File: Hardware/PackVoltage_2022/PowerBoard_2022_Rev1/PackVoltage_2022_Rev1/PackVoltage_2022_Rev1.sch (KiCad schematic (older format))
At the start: 20 parts

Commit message: added andersons
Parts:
- added Conn? (x2): M1, symbol MRDT_Connectors:AndersonPP
- added Conn? (x2): M2, symbol MRDT_Connectors:AndersonPP
- added Conn? (x2): M3, symbol MRDT_Connectors:AndersonPP
- added Conn? (x2): M4, symbol MRDT_Connectors:AndersonPP
- added Conn? (x2): M5, symbol MRDT_Connectors:AndersonPP
- added Conn? (x2): M6, symbol MRDT_Connectors:AndersonPP
- added Conn? (x2): Spare, symbol MRDT_Connectors:AndersonPP
- C? (x4): value CP1 -> 470uF
- D? (x2): value D -> 1.5KE36A+
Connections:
- net GND: now also Conn?.1 (GND), Conn?.1 (GND), Conn?.1 (GND), Conn?.1 (GND), Conn?.1 (GND), Conn?.1 (GND), Conn?.1 (GND)
- new net Anderson_M1: Conn?.4 (PV+)
- new net Anderson_M2: Conn?.4 (PV+)
- new net Anderson_M3: Conn?.4 (PV+)
- new net Anderson_M4: Conn?.4 (PV+)
- new net Anderson_M5: Conn?.4 (PV+)
- new net Anderson_M6: Conn?.4 (PV+)
- new net Anderson_Spare: Conn?.4 (PV+)
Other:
- moved on the sheet: C?, D?, R?

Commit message: fixed anderson tags
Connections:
- net Anderson_M1 renamed MOTORS/Anderson_M1
- net Anderson_M2 renamed MOTORS/Anderson_M2
- net Anderson_M3 renamed MOTORS/Anderson_M3
- net Anderson_M4 renamed MOTORS/Anderson_M4
- net Anderson_M5 renamed MOTORS/Anderson_M5
- net Anderson_M6 renamed MOTORS/Anderson_M6
- net Anderson_Spare renamed MOTORS/Anderson_Spare
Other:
- moved on the sheet: Conn?A, Conn?D

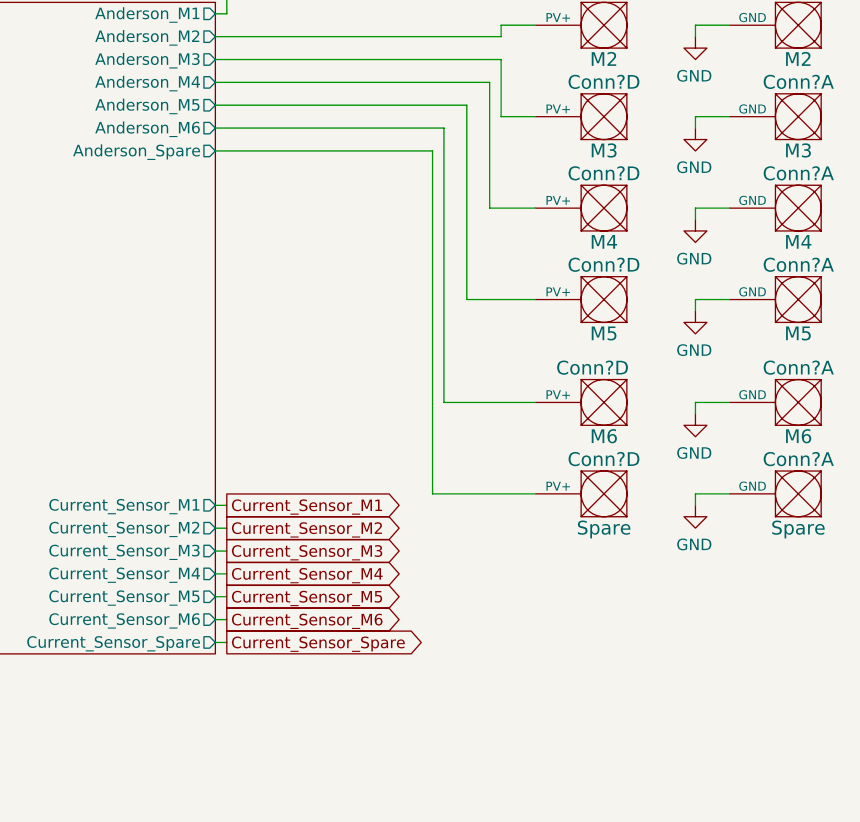
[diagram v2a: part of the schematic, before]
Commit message: added 12V anderson
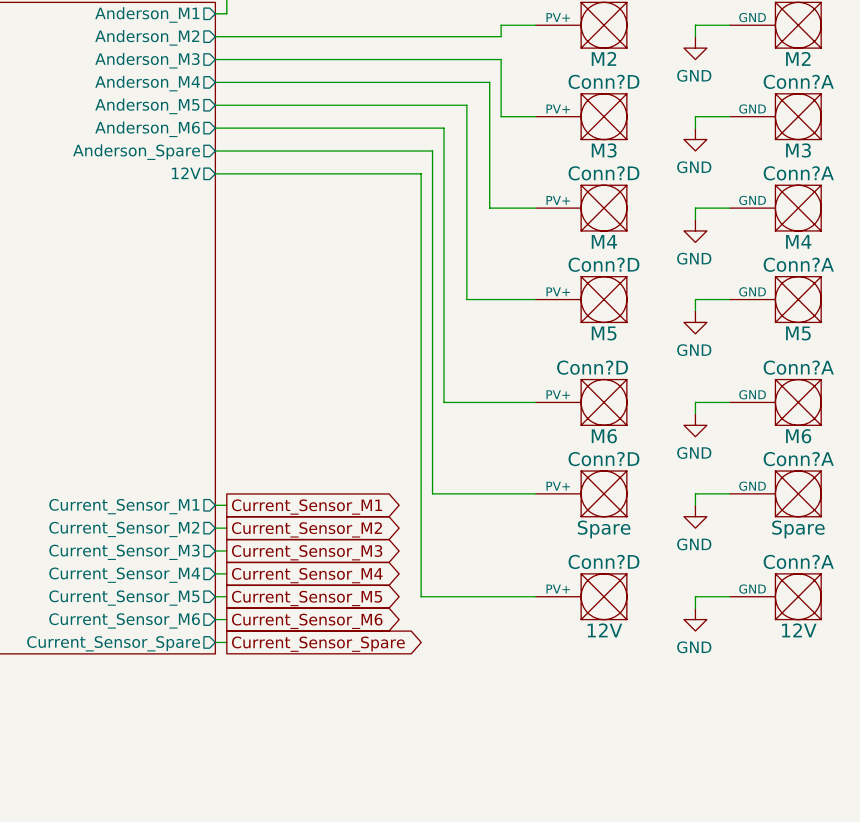
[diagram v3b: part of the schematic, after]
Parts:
- added Conn? (x2): 12V, symbol MRDT_Connectors:AndersonPP
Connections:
- net GND: now also Conn?.1 (GND)
- new net MOTORS/12V: Conn?.4 (PV+)
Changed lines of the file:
@@
 F23 "Current_Sensor_M3" O R 8300 3350 50
 F24 "Current_Sensor_M4" O R 8300 3450 50
+F25 "12V" O R 8300 1700 50
 $EndSheet
 $Comp
@@
 Wire Wire Line
 	9250 3100 9700 3100
+$Comp
+L MRDT_Connectors:AndersonPP Conn?
+U 1 1 6243818E
+P 10950 3650
+F 0 "Conn?" H 11050 3900 60  0000 C CNN
+F 1 "12V" H 11050 3600 60  0000 C CNN
+F 2 "" H 10800 3100 60  0001 C CNN
+F 3 "" H 10800 3100 60  0001 C CNN
+	1    10950 3650
+	-1   0    0    -1
+$EndComp
+$Comp
+L MRDT_Connectors:AndersonPP Conn?
+U 4 1 62438195
+P 10100 3650
+F 0 "Conn?" H 10200 3900 60  0000 C CNN
+F 1 "12V" H 10200 3600 60  0000 C CNN
+F 2 "" H 9950 3100 60  0001 C CNN
+F 3 "" H 9950 3100 60  0001 C CNN
+	4    10100 3650
+	-1   0    0    -1
+$EndComp
+Wire Wire Line
+	10550 3550 10400 3550
+Wire Wire Line
+	10400 3550 10400 3600
+$Comp
+L power:GND #PWR?
+U 1 1 6243819E
+P 10400 3600
+F 0 "#PWR?" H 10400 3350 50  0001 C CNN
+F 1 "GND" H 10405 3427 50  0000 C CNN
+F 2 "" H 10400 3600 50  0001 C CNN
+F 3 "" H 10400 3600 50  0001 C CNN
+	1    10400 3600
+	-1   0    0    -1
+$EndComp
+Wire Wire Line
+	8300 1700 9200 1700
+Wire Wire Line
+	9200 1700 9200 3550
+Wire Wire Line
+	9200 3550 9700 3550
 $EndSCHEMATC

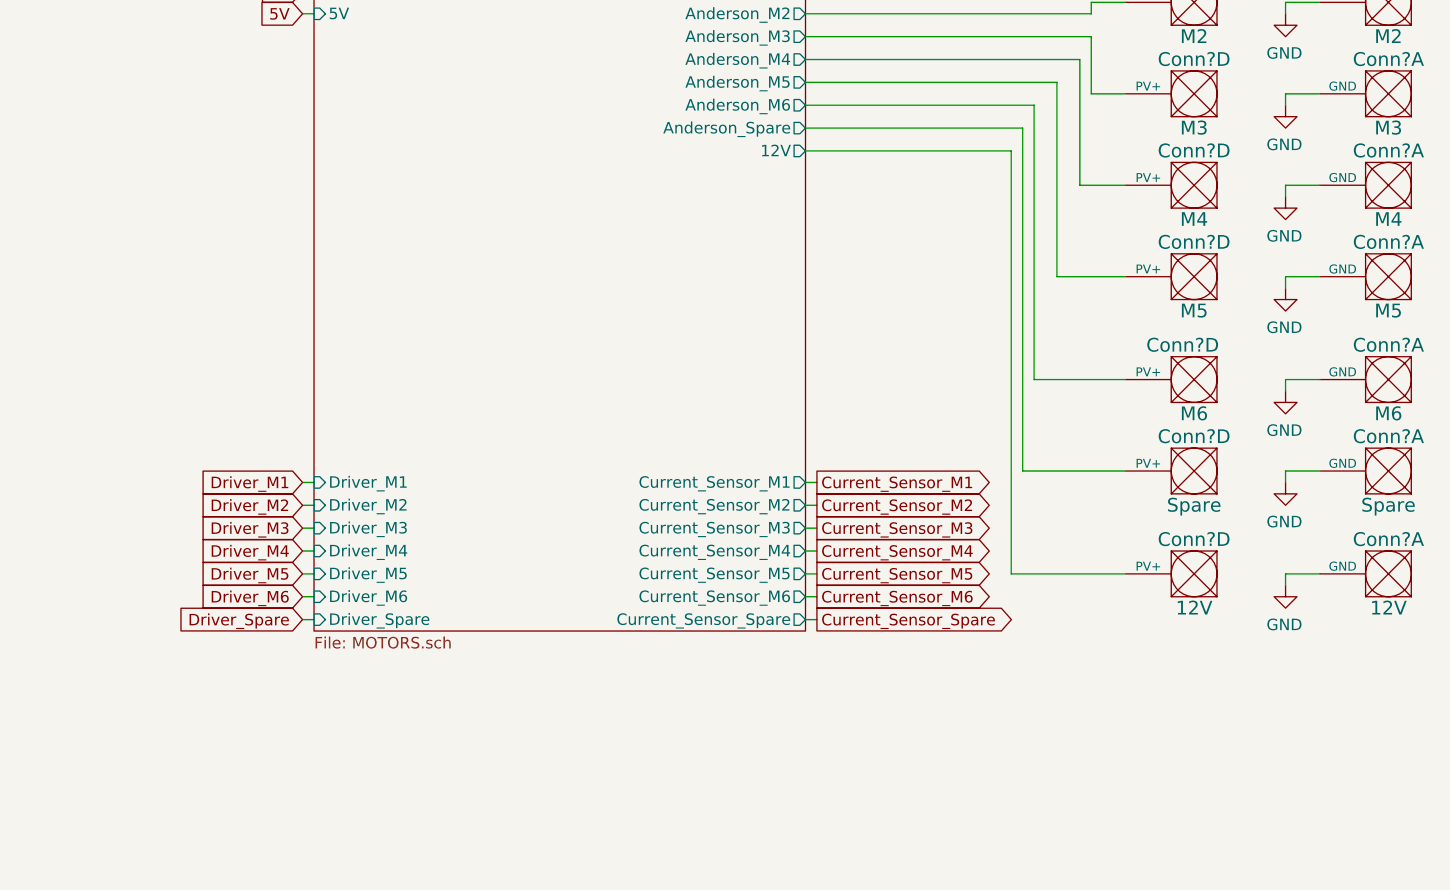
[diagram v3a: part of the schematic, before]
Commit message: Added POE
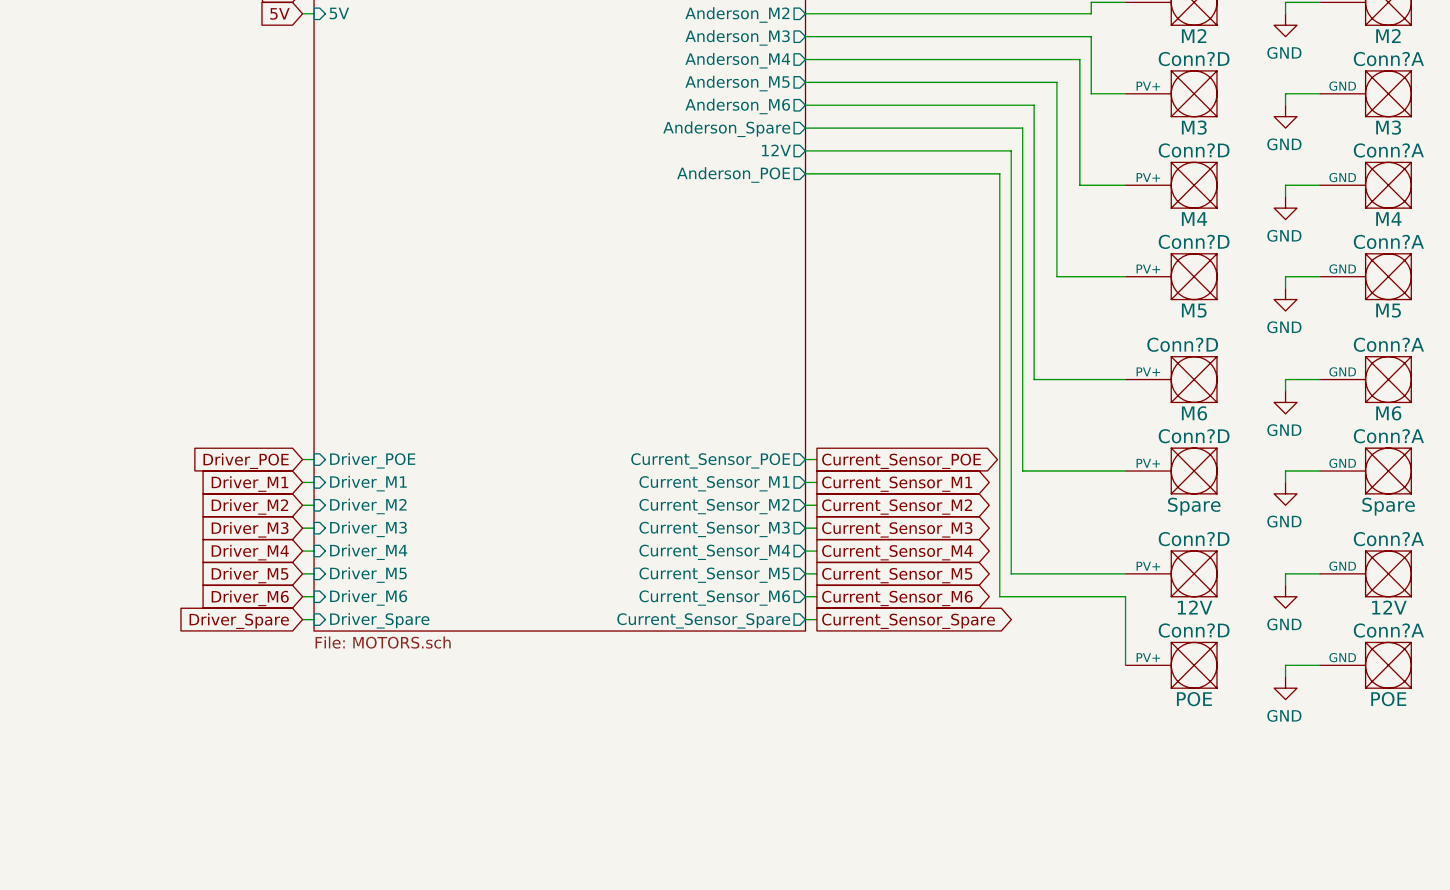
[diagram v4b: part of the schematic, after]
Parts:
- added Conn? (x2): POE, symbol MRDT_Connectors:AndersonPP
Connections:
- net GND: now also Conn?.1 (GND)
- new net MOTORS/Anderson_POE: Conn?.4 (PV+)
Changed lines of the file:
@@
 EESchema Schematic File Version 4
+LIBS:PackVoltage_2022_Rev1-cache
 EELAYER 26 0
 EELAYER END
@@
 F24 "Current_Sensor_M4" O R 8300 3450 50
 F25 "12V" O R 8300 1700 50
+F26 "Driver_POE" I L 6150 3050 50
+F27 "Anderson_POE" O R 8300 1800 50
+F28 "Current_Sensor_POE" O R 8300 3050 50
 $EndSheet
 $Comp
@@
 Wire Wire Line
 	9200 3550 9700 3550
+$Comp
+L MRDT_Connectors:AndersonPP Conn?
+U 1 1 6213C762
+P 10950 4050
+F 0 "Conn?" H 11050 4300 60  0000 C CNN
+F 1 "POE" H 11050 4000 60  0000 C CNN
+F 2 "" H 10800 3500 60  0001 C CNN
+F 3 "" H 10800 3500 60  0001 C CNN
+	1    10950 4050
+	-1   0    0    -1
+$EndComp
+$Comp
+L MRDT_Connectors:AndersonPP Conn?
+U 4 1 6213C769
+P 10100 4050
+F 0 "Conn?" H 10200 4300 60  0000 C CNN
+F 1 "POE" H 10200 4000 60  0000 C CNN
+F 2 "" H 9950 3500 60  0001 C CNN
+F 3 "" H 9950 3500 60  0001 C CNN
+	4    10100 4050
+	-1   0    0    -1
+$EndComp
+Wire Wire Line
+	10550 3950 10400 3950
+Wire Wire Line
+	10400 3950 10400 4000
+$Comp
+L power:GND #PWR?
+U 1 1 6213C772
+P 10400 4000
+F 0 "#PWR?" H 10400 3750 50  0001 C CNN
+F 1 "GND" H 10405 3827 50  0000 C CNN
+F 2 "" H 10400 4000 50  0001 C CNN
+F 3 "" H 10400 4000 50  0001 C CNN
+	1    10400 4000
+	-1   0    0    -1
+$EndComp
+Wire Wire Line
+	8300 3050 8350 3050
+Text GLabel 8350 3050 2    50   Output ~ 0
+Current_Sensor_POE
+Text GLabel 6100 3050 0    50   Input ~ 0
+Driver_POE
+Wire Wire Line
+	6100 3050 6150 3050
+Wire Wire Line
+	8300 1800 9150 1800
+Wire Wire Line
+	9150 1800 9150 3650
+Wire Wire Line
+	9150 3650 9700 3650
+Wire Wire Line
+	9700 3650 9700 3950
 $EndSCHEMATC

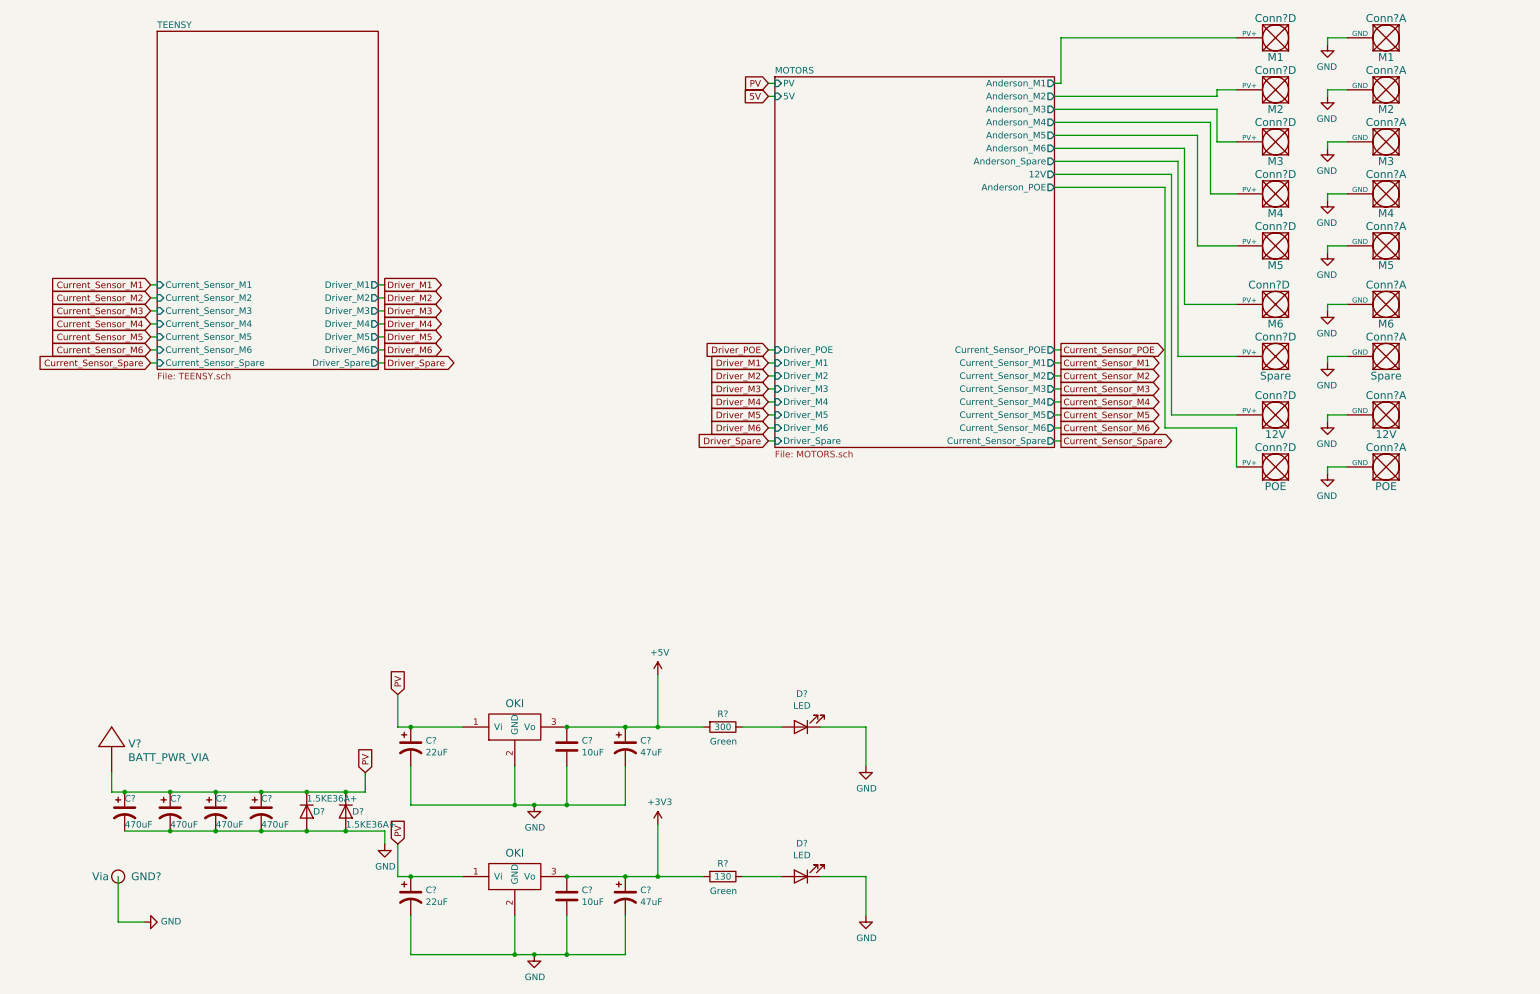
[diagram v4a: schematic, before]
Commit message: Cleaned up main page and added POE Current sense and driver
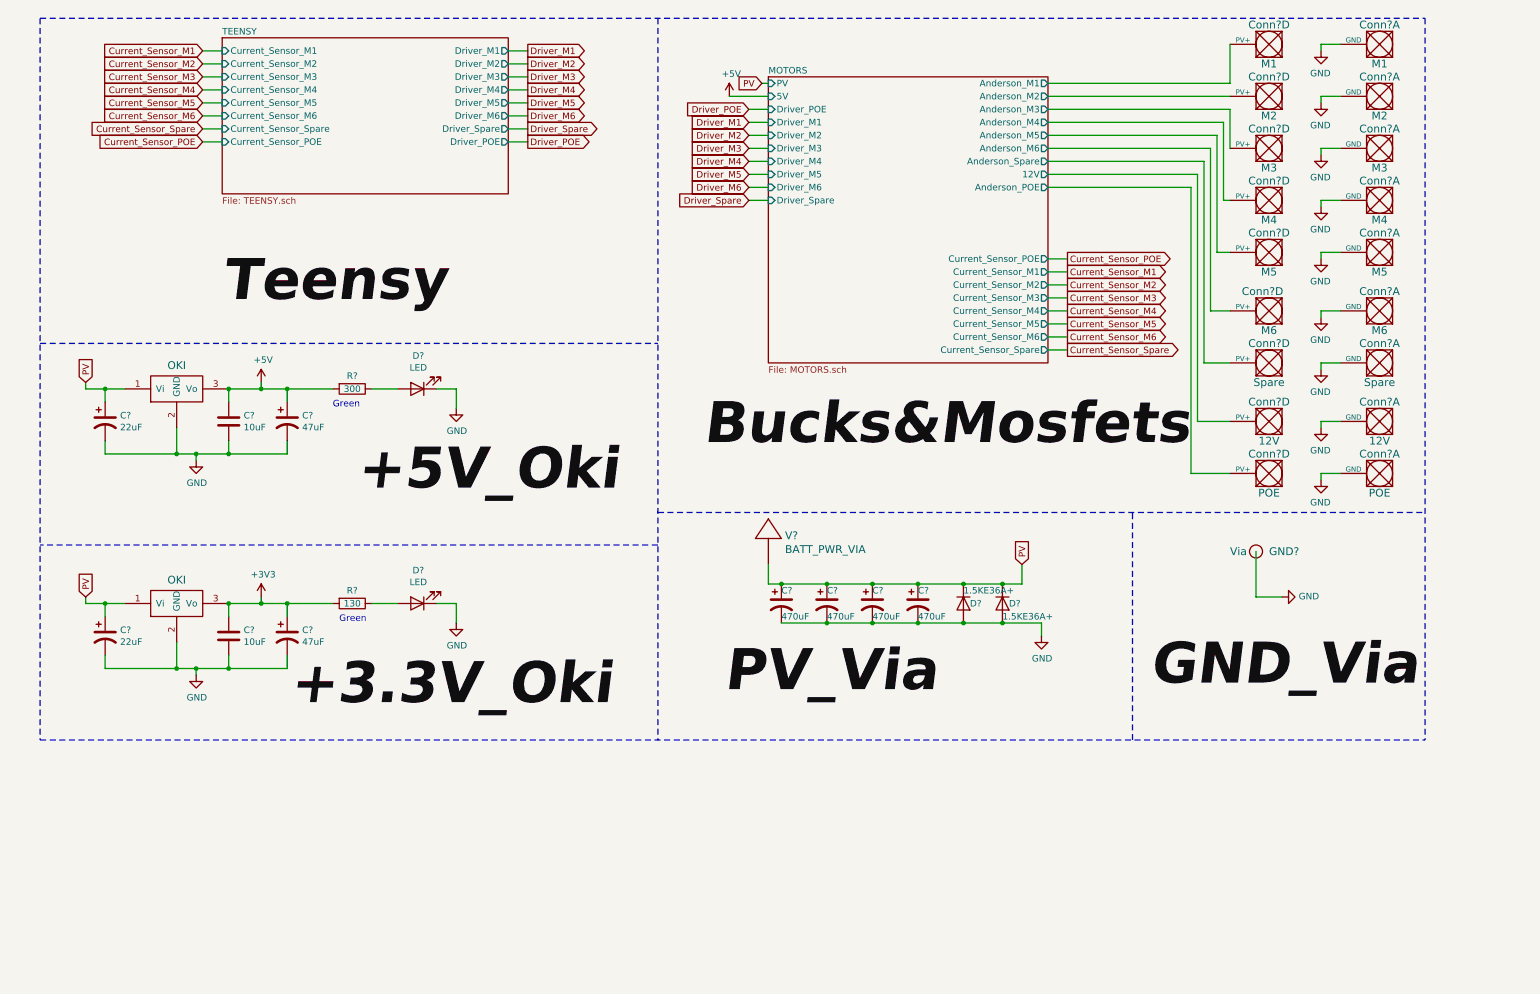
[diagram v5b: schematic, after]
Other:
- moved on the sheet: C?, Conn?A, Conn?D, D?, GND?, R?, V?

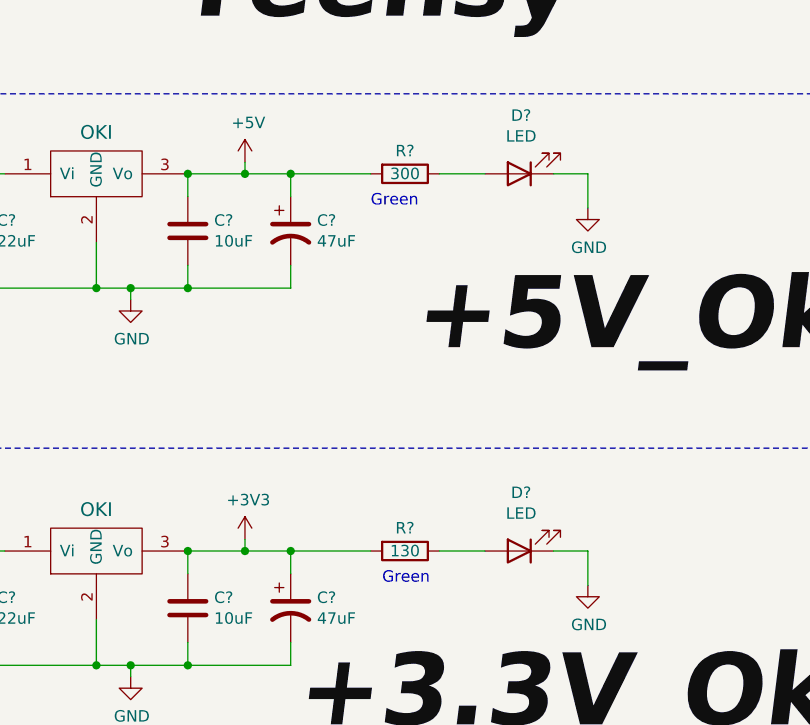
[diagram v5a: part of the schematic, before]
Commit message: Changed resistor values pt.1
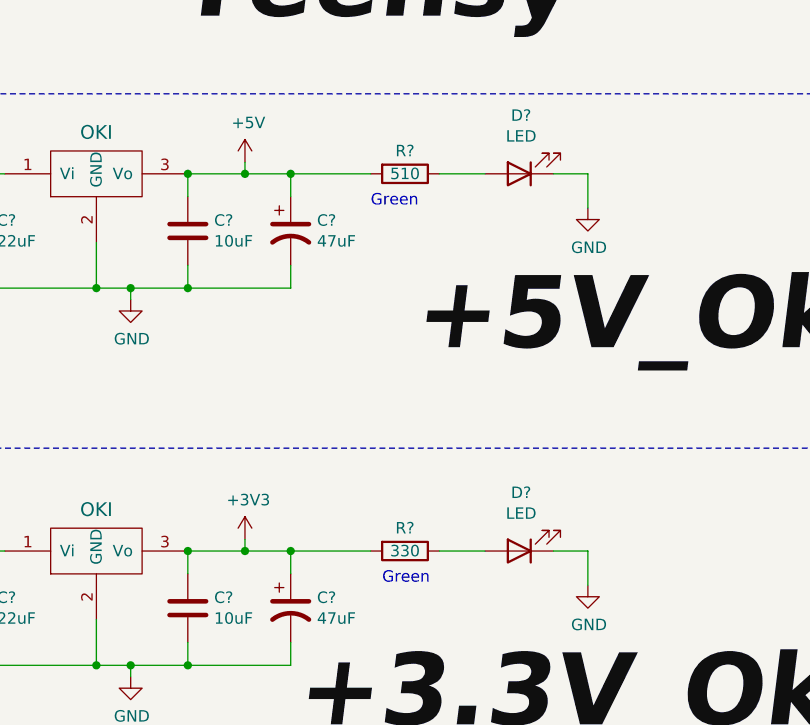
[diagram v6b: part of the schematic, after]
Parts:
- R?: value 300 -> 510
- R?: value 130 -> 330
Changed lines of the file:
@@
 AR Path="/62196DEB" Ref="R?"  Part="1"
 F 0 "R?" V 2800 3350 50  0000 C CNN
-F 1 "300" V 2900 3350 50  0000 C CNN
+F 1 "510" V 2900 3350 50  0000 C CNN
 F 2 "" V 2830 3350 50  0001 C CNN
 F 3 "~" H 2900 3350 50  0001 C CNN
@@
 AR Path="/62196E3C" Ref="R?"  Part="1"
 F 0 "R?" V 2800 5000 50  0000 C CNN
-F 1 "130" V 2900 5000 50  0000 C CNN
+F 1 "330" V 2900 5000 50  0000 C CNN
 F 2 "" V 2830 5000 50  0001 C CNN
 F 3 "~" H 2900 5000 50  0001 C CNN

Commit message: Named the board
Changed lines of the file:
@@
 Text Label 11100 5700 2    315  Italic 63
 GND_Via
+Text Label 7100 6800 0    157  Italic 31
+PackVoltage_PowerBoard
+Text Label 7100 7100 0    157  Italic 31
+"Rev3"
 $EndSCHEMATC
